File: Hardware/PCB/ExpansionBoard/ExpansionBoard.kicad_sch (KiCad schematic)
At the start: 0 parts

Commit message: INT BUS
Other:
- sheet Accelerometer.Sheet ports: added INT; removed none
- sheet MCU Sheet ports: added INT; removed none
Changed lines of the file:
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@@
+		)
+	)
+	(wire
+		(pts
+			(xy 110.49 63.5) (xy 133.35 63.5)
+		)
+		(stroke
+			(width 0)
+			(type default)
 		)
 	)
@@
 		(pin "SPI" bidirectional
 			(at 110.49 54.61 0)
+			(effects
+				(font
+					(size 1.27 1.27)
+				)
+				(justify right)
+			)
+		)
+		(pin "INT" output
+			(at 110.49 63.5 0)
 			(effects
 				(font
@@
 			(effects
 				(font
+					(size 1.27 1.27)
+				)
+				(justify left)
+			)
+		)
+		(pin "INT" input
+			(at 133.35 63.5 180)
+			(effects
+				(font

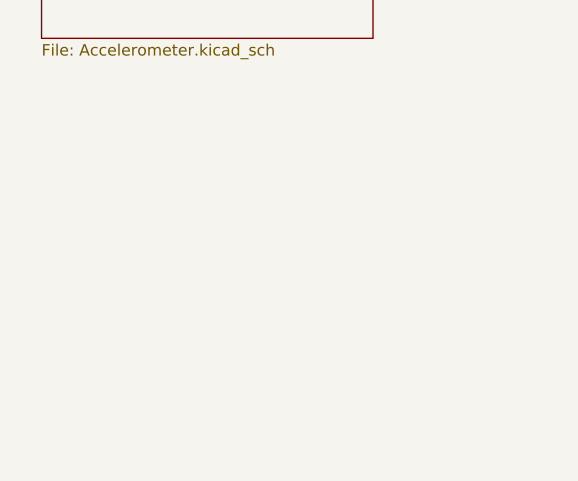
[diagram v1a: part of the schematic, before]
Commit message: added POWER Sheet
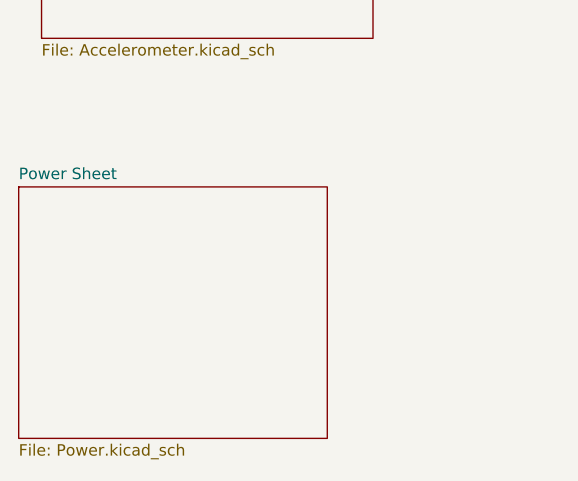
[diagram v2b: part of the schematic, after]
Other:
- added sheet Power Sheet (Power.kicad_sch)
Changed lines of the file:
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@@
+	)
+	(sheet
+		(at 71.12 99.06)
+		(size 34.29 27.94)
+		(fields_autoplaced yes)
+		(stroke
+			(width 0.1524)
+			(type solid)
+		)
+		(fill
+			(color 0 0 0 0.0000)
+		)
+		(property "Sheetname" "Power Sheet"
+			(at 71.12 98.3484 0)
+			(effects
+				(font
+					(size 1.27 1.27)
+				)
+				(justify left bottom)
+			)
+		)
+		(property "Sheetfile" "Power.kicad_sch"
+			(at 71.12 127.5846 0)
+			(effects
+				(font
+					(size 1.27 1.27)
+				)
+				(justify left top)
+			)
+		)
+		(instances
+			(project "ExpansionBoard"
+				(path "/fb49e4b5-d7b7-45bf-8a57-314a3950416b"
+					(page "4")
+				)
+			)
+		)
 	)
 	(sheet

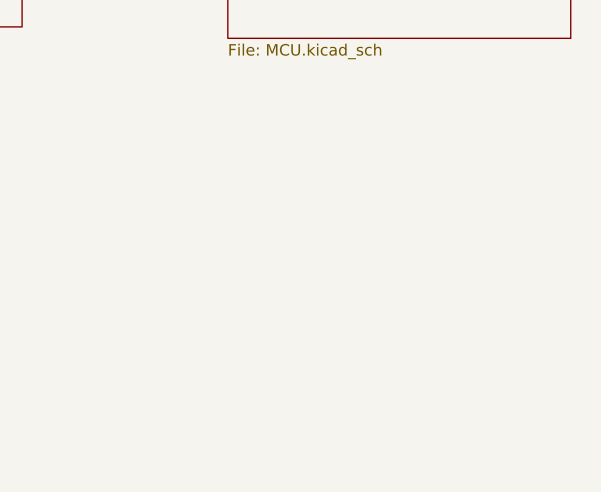
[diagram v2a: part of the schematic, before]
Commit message: added PINOUT to mcu and UART USB CHIP
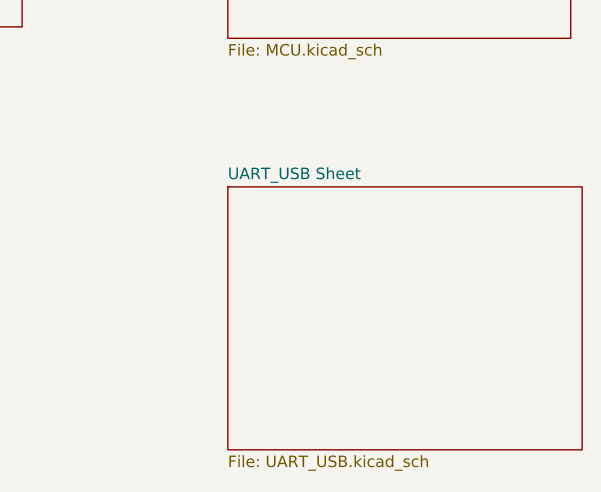
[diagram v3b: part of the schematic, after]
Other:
- added sheet UART_USB Sheet (UART_USB.kicad_sch)
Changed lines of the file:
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@@
+	)
+	(sheet
+		(at 133.35 100.33)
+		(size 39.37 29.21)
+		(fields_autoplaced yes)
+		(stroke
+			(width 0.1524)
+			(type solid)
+		)
+		(fill
+			(color 0 0 0 0.0000)
+		)
+		(property "Sheetname" "UART_USB Sheet"
+			(at 133.35 99.6184 0)
+			(effects
+				(font
+					(size 1.27 1.27)
+				)
+				(justify left bottom)
+			)
+		)
+		(property "Sheetfile" "UART_USB.kicad_sch"
+			(at 133.35 130.1246 0)
+			(effects
+				(font
+					(size 1.27 1.27)
+				)
+				(justify left top)
+			)
+		)
+		(instances
+			(project "ExpansionBoard"
+				(path "/fb49e4b5-d7b7-45bf-8a57-314a3950416b"
+					(page "5")
+				)
+			)
+		)
 	)
 	(sheet

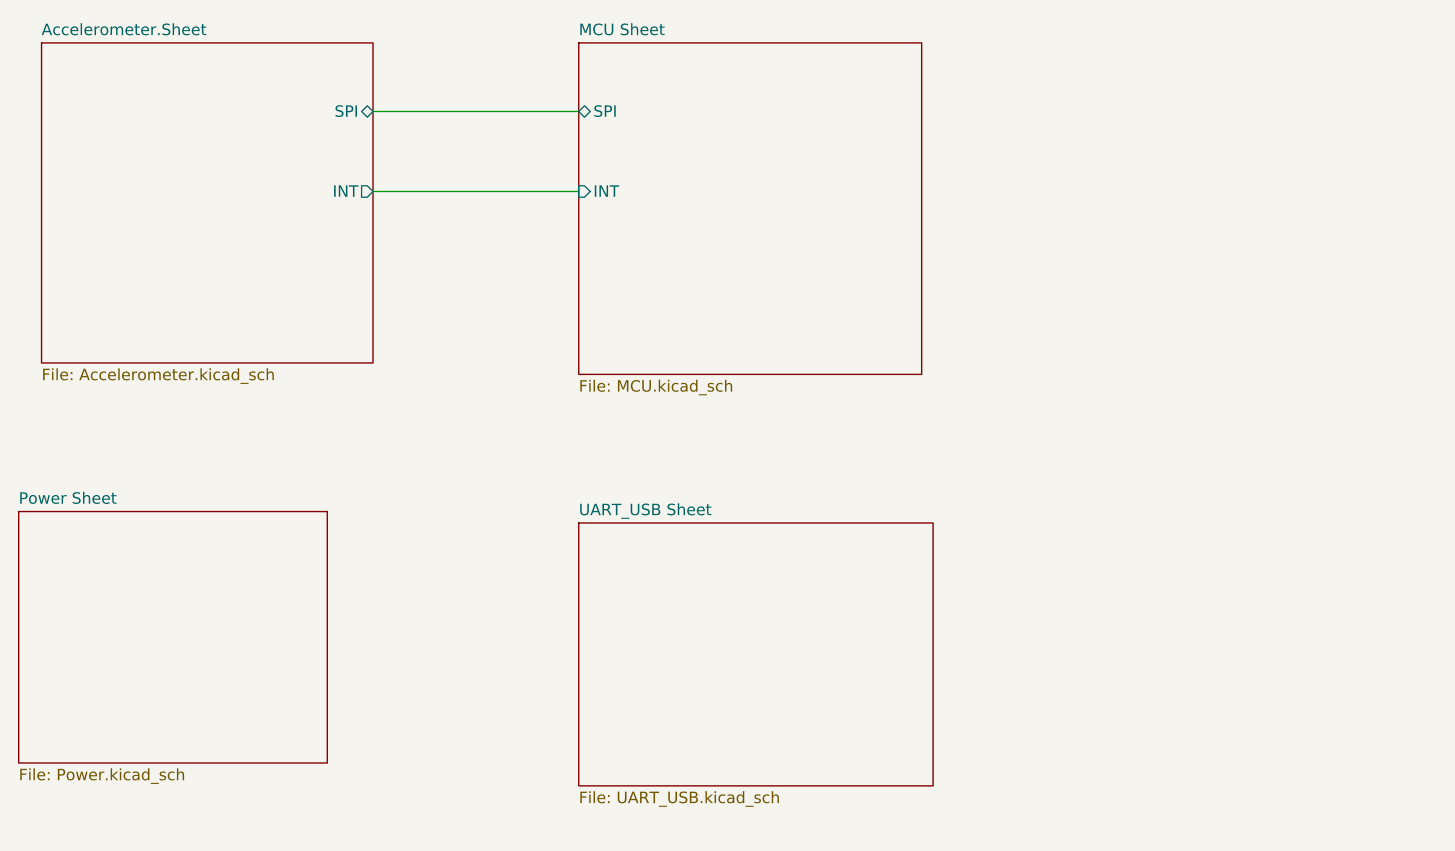
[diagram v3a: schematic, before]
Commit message: DONE: PWR LED MISSING AND AIRSPEED
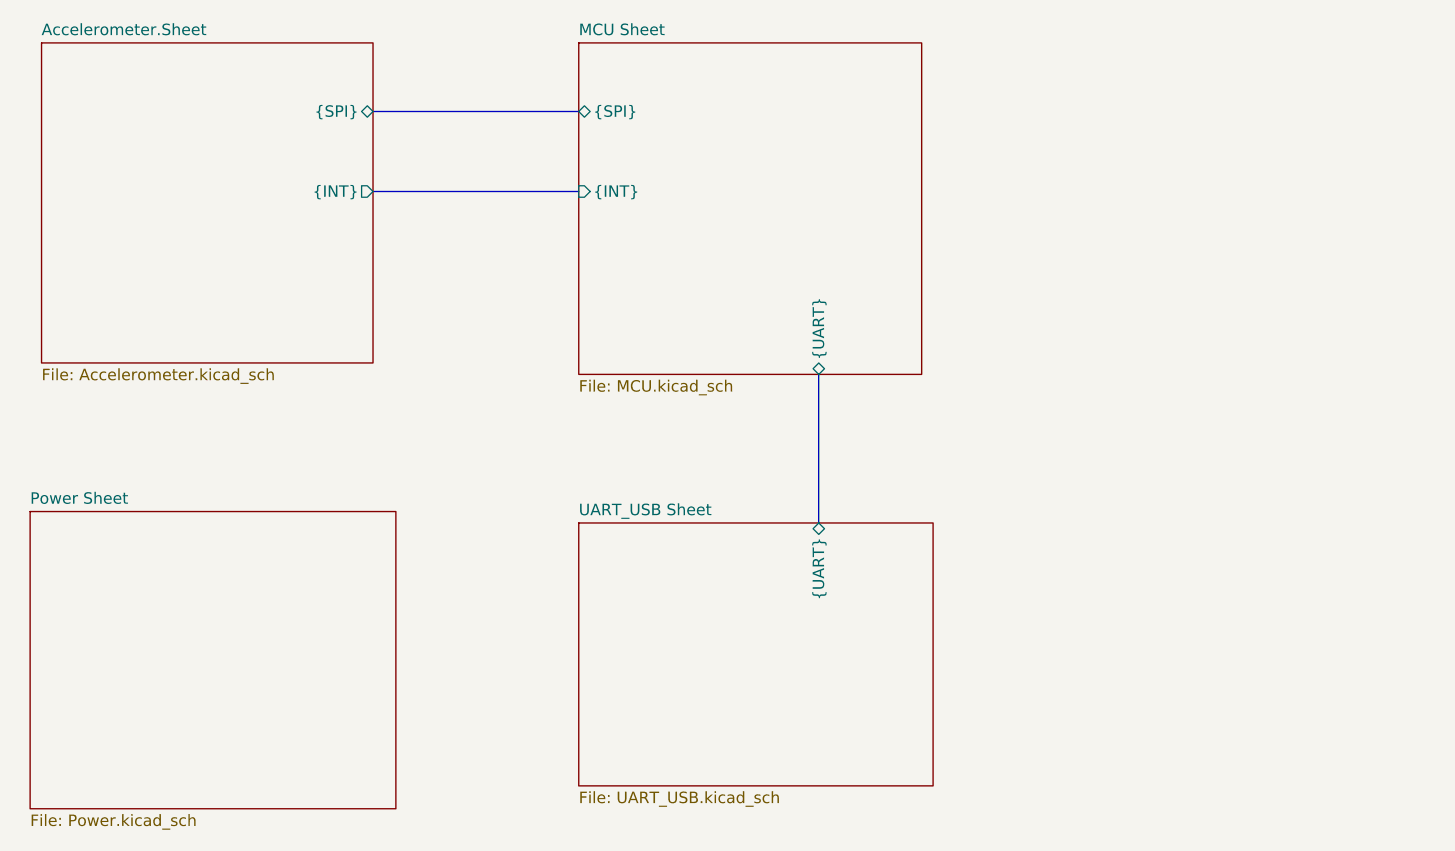
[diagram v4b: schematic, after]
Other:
- sheet Accelerometer.Sheet ports: added {INT}, {SPI}; removed INT, SPI
- sheet MCU Sheet ports: added {INT}, {SPI}, {UART}; removed INT, SPI
- sheet UART_USB Sheet ports: added {UART}; removed none
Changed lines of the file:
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@@
 	(generator_version "8.0")
 	(paper "A4")
-	(wire
+	(bus
+		(pts
+			(xy 160.02 83.82) (xy 160.02 100.33)
+		)
+		(stroke
+			(width 0)
+			(type default)
+		)
+	)
+	(bus
+		(pts
+			(xy 110.49 63.5) (xy 133.35 63.5)
+		)
+		(stroke
+			(width 0)
+			(type default)
+		)
+	)
+	(bus
 		(pts
 			(xy 110.49 54.61) (xy 133.35 54.61)
@@
 		)
 	)
-	(wire
-		(pts
-			(xy 110.49 63.5) (xy 133.35 63.5)
-		)
-		(stroke
-			(width 0)
-			(type default)
-		)
-	)
 	(sheet
 		(at 133.35 100.33)
@@
 				)
 				(justify left top)
+			)
+		)
+		(pin "{UART}" bidirectional
+			(at 160.02 100.33 90)
+			(effects
+				(font
+					(size 1.27 1.27)
+				)
+				(justify right)
 			)
 		)
@@
 	)
 	(sheet
-		(at 71.12 99.06)
-		(size 34.29 27.94)
+		(at 72.39 99.06)
+		(size 40.64 33.02)
 		(fields_autoplaced yes)
 		(stroke
@@
 		)
 		(property "Sheetname" "Power Sheet"
-			(at 71.12 98.3484 0)
+			(at 72.39 98.3484 0)
 			(effects
 				(font
@@
 		)
 		(property "Sheetfile" "Power.kicad_sch"
-			(at 71.12 127.5846 0)
+			(at 72.39 132.6646 0)
 			(effects
 				(font
@@
 			)
 		)
-		(pin "SPI" bidirectional
+		(pin "{SPI}" bidirectional
 			(at 110.49 54.61 0)
 			(effects
@@
 			)
 		)
-		(pin "INT" output
+		(pin "{INT}" output
 			(at 110.49 63.5 0)
 			(effects
@@
 			)
 		)
-		(pin "SPI" bidirectional
+		(pin "{SPI}" bidirectional
 			(at 133.35 54.61 180)
 			(effects
@@
 			)
 		)
-		(pin "INT" input
+		(pin "{INT}" input
 			(at 133.35 63.5 180)
 			(effects
 				(font
+					(size 1.27 1.27)
+				)
+				(justify left)
+			)
+		)
+		(pin "{UART}" bidirectional
+			(at 160.02 83.82 270)
+			(effects
+				(font

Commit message: added Airspeed simulation and Footprint with 3D model
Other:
- added sheet Airspeed Sheet (Airspeed.kicad_sch)
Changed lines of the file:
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@@
+	)
+	(sheet
+		(at 187.96 46.99)
+		(size 40.64 36.83)
+		(fields_autoplaced yes)
+		(stroke
+			(width 0.1524)
+			(type solid)
+		)
+		(fill
+			(color 0 0 0 0.0000)
+		)
+		(property "Sheetname" "Airspeed Sheet"
+			(at 187.96 46.2784 0)
+			(effects
+				(font
+					(size 1.27 1.27)
+				)
+				(justify left bottom)
+			)
+		)
+		(property "Sheetfile" "Airspeed.kicad_sch"
+			(at 187.96 84.4046 0)
+			(effects
+				(font
+					(size 1.27 1.27)
+				)
+				(justify left top)
+			)
+		)
+		(instances
+			(project "ExpansionBoard"
+				(path "/fb49e4b5-d7b7-45bf-8a57-314a3950416b"
+					(page "6")
+				)
+			)
+		)
 	)
 	(sheet

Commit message: finished schema
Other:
- sheet Airspeed Sheet ports: added {Airspeed_I2C}; removed none
- sheet MCU Sheet ports: added {Airspeed_I2C}; removed none
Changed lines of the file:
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@@
+	(bus
+		(pts
+			(xy 171.45 54.61) (xy 187.96 54.61)
+		)
+		(stroke
+			(width 0)
+			(type default)
+		)
+	)
 	(bus
 		(pts
@@
 			)
 		)
+		(pin "{Airspeed_I2C}" bidirectional
+			(at 187.96 54.61 180)
+			(effects
+				(font
+					(size 1.27 1.27)
+				)
+				(justify left)
+			)
+		)
 		(instances
 			(project "ExpansionBoard"
@@
 			)
 		)
+		(pin "{Airspeed_I2C}" bidirectional
+			(at 171.45 54.61 0)
+			(effects
+				(font
+					(size 1.27 1.27)
+				)
+				(justify right)
+			)
+		)

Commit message: added Cube Project, SD Card and Tillt Switch
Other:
- sheet Accelerometer.Sheet ports: added Angle_Indicator_1, Angle_Indicator_2; removed none
- sheet MCU Sheet ports: added Angle_Indicator_1, Angle_Indicator_2; removed none
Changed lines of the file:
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@@
+		)
+	)
+	(wire
+		(pts
+			(xy 110.49 69.85) (xy 133.35 69.85)
+		)
+		(stroke
+			(width 0)
+			(type default)
 		)
 	)
@@
 		(pts
 			(xy 110.49 54.61) (xy 133.35 54.61)
+		)
+		(stroke
+			(width 0)
+			(type default)
+		)
+	)
+	(wire
+		(pts
+			(xy 110.49 72.39) (xy 133.35 72.39)
 		)
 		(stroke
@@
 			)
 		)
+		(pin "Angle_Indicator_1" output
+			(at 110.49 69.85 0)
+			(effects
+				(font
+					(size 1.27 1.27)
+				)
+				(justify right)
+			)
+		)
+		(pin "Angle_Indicator_2" output
+			(at 110.49 72.39 0)
+			(effects
+				(font
+					(size 1.27 1.27)
+				)
+				(justify right)
+			)
+		)
 		(instances
 			(project "ExpansionBoard"
@@
 			)
 		)
+		(pin "Angle_Indicator_2" input
+			(at 133.35 72.39 180)
+			(effects
+				(font
+					(size 1.27 1.27)
+				)
+				(justify left)
+			)
+		)
+		(pin "Angle_Indicator_1" input
+			(at 133.35 69.85 180)
+			(effects
+				(font
+					(size 1.27 1.27)
+				)
+				(justify left)
+			)
+		)
